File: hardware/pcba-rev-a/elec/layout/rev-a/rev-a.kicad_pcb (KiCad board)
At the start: 4 copper layers, 160 x 100 mm, 154 parts

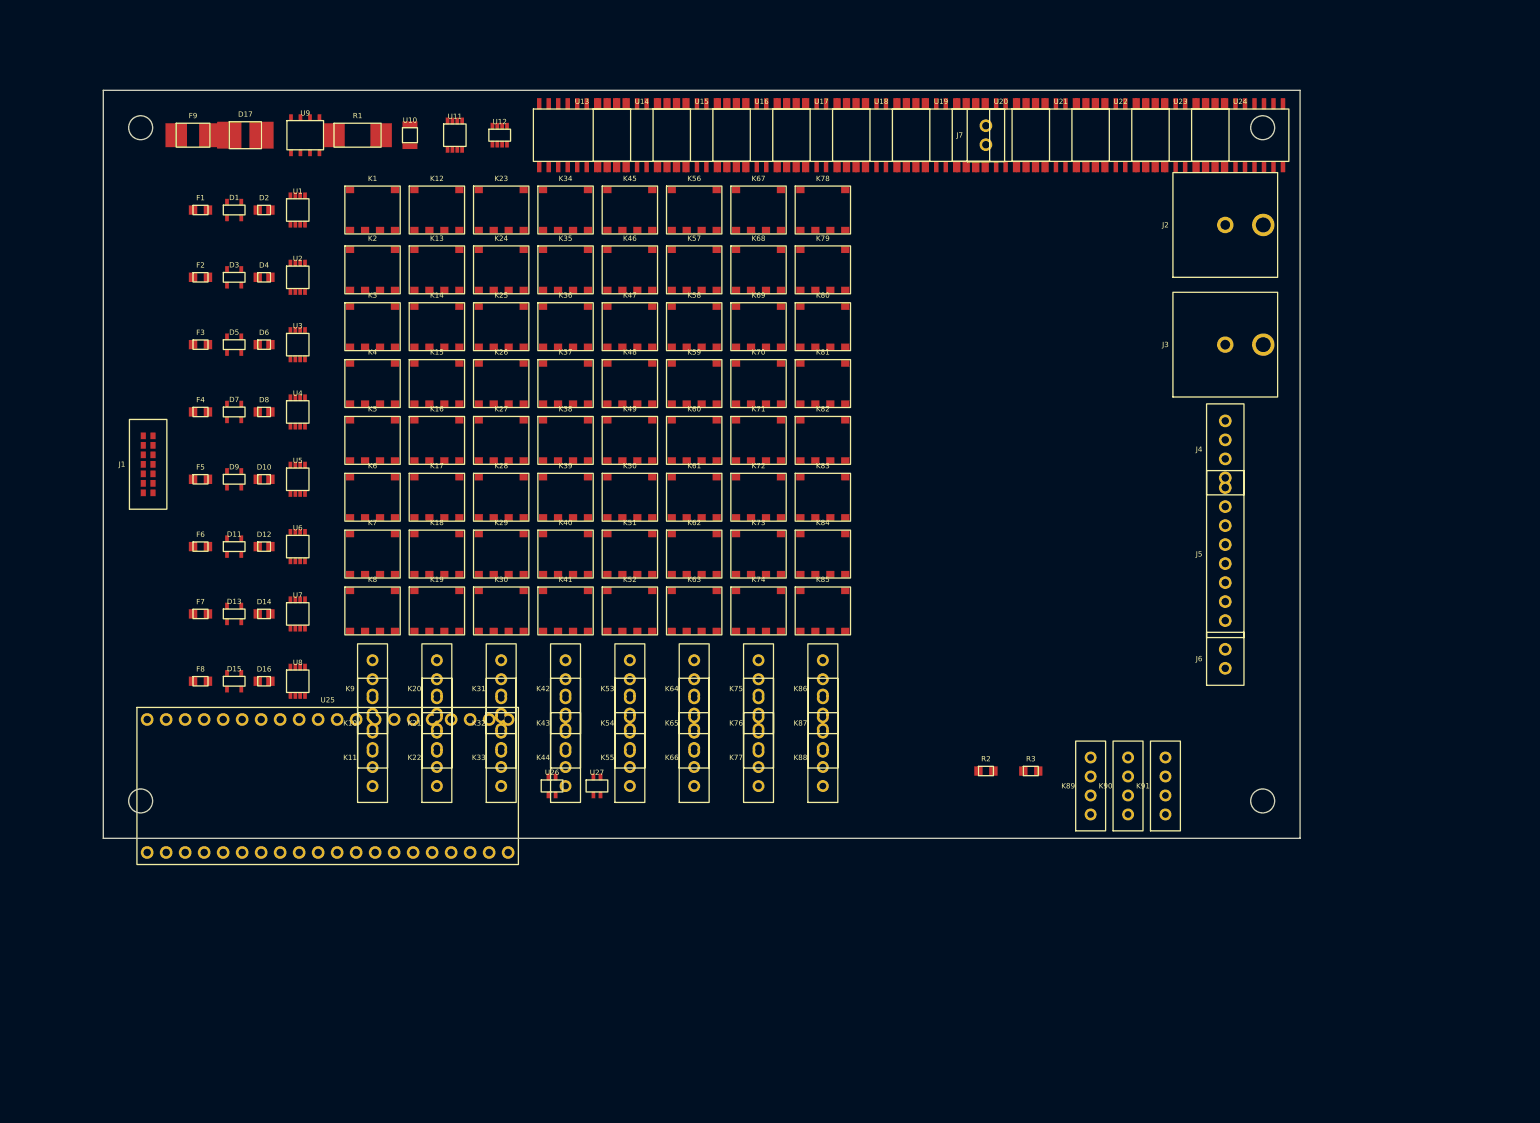
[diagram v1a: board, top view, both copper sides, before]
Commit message: Rev A board: real KiCad library footprints, 3D bodies, DRC-clean floorplan
- gen_board.py now instantiates KiCad's installed library footprints
  (Omron G6K-2F-Y, StandexMeder SIL reed, SOIC-20W, Pico 2 module,
  Amphenol BNC, headers, passives) with nets injected into their pads -
  3D viewer shows actual component bodies.
- Board grown 160x100 -> 200x146: measured courtyards total ~12,100 mm2
  (76% utilization on the old outline - unplaceable). Iterated against
  kicad-cli DRC to zero courtyard overlaps and zero edge violations
  (was 126 + 7 on first pass; bugs: Pico rotated long-axis horizontal,
  sink pitch vs BNCs, relay field touching reed bank, header rotations).
- project_spec.json outline updated with rationale.

Co-Authored-By: Claude Fable 5 <noreply@anthropic.com>
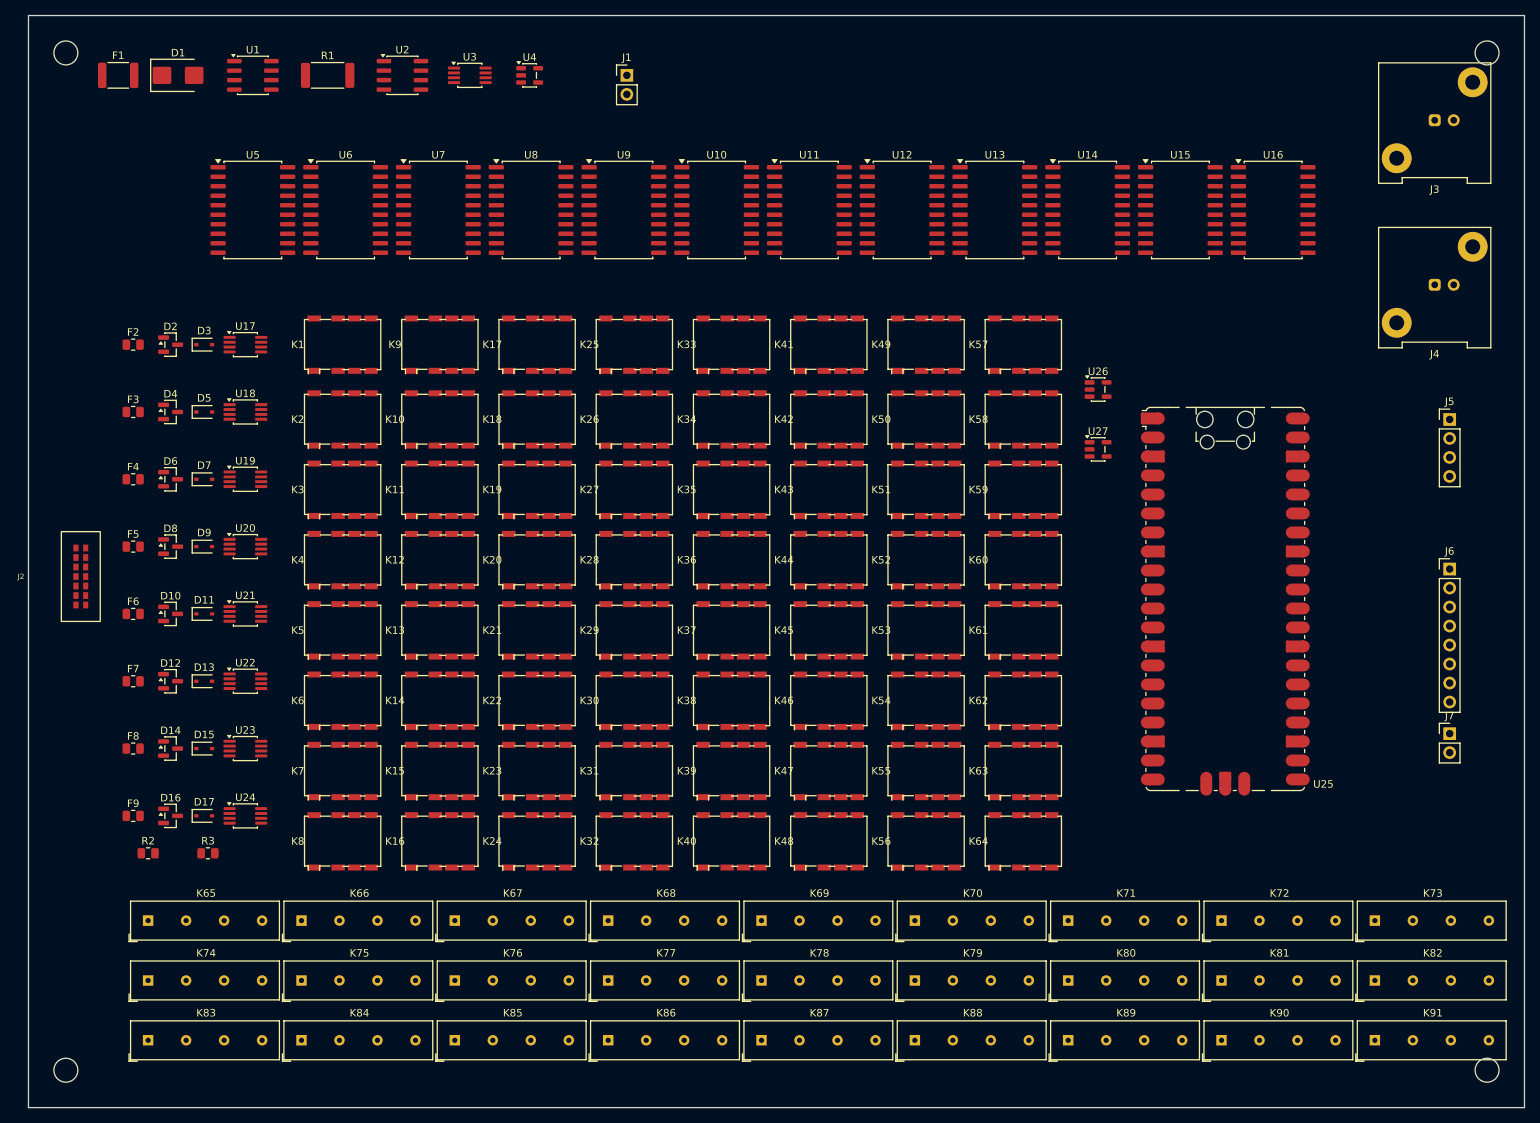
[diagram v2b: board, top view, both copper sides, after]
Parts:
- D1: value (none) -> D_SMB; footprint EE:SOT23 -> Diode_SMD:D_SMB
- D10, D12, D14, D16, D2, D4, D6, D8: value (none) -> SOT-23; footprint EE:SOD323 -> Package_TO_SOT_SMD:SOT-23
- D11, D13, D15, D3, D5, D7, D9: value (none) -> D_SOD-323; footprint EE:SOT23 -> Diode_SMD:D_SOD-323
- D17: value (none) -> D_SOD-323; footprint EE:SMB -> Diode_SMD:D_SOD-323
- F1: value (none) -> Fuse_1812_4532Metric; footprint EE:PTC0805 -> Fuse:Fuse_1812_4532Metric
- F2, F3, F4, F5, F6, F7, F8: value (none) -> R_0805_2012Metric; footprint EE:PTC0805 -> Resistor_SMD:R_0805_2012Metric
- F9: value (none) -> R_0805_2012Metric; footprint EE:FUSE1812 -> Resistor_SMD:R_0805_2012Metric
- J1: value (none) -> PinHeader_1x02_P2.54mm_Vertical; footprint EE:SEAF14 -> Connector_PinHeader_2.54mm:PinHeader_1x02_P2.54mm_Vertical
- J2: footprint EE:BNC_TH -> EE:SEAF14
- J3: value (none) -> BNC_Amphenol_031-5539_Vertical; footprint EE:BNC_TH -> Connector_Coaxial:BNC_Amphenol_031-5539_Vertical
- J4: value (none) -> BNC_Amphenol_031-5539_Vertical; footprint EE:HDR4 -> Connector_Coaxial:BNC_Amphenol_031-5539_Vertical
- J5: value (none) -> PinHeader_1x04_P2.54mm_Vertical; footprint EE:HDR8 -> Connector_PinHeader_2.54mm:PinHeader_1x04_P2.54mm_Vertical
- J6: value (none) -> PinHeader_1x08_P2.54mm_Vertical; footprint EE:HDR2 -> Connector_PinHeader_2.54mm:PinHeader_1x08_P2.54mm_Vertical
- J7: value (none) -> PinHeader_1x02_P2.54mm_Vertical; footprint EE:HDR2 -> Connector_PinHeader_2.54mm:PinHeader_1x02_P2.54mm_Vertical
- K1, K12, K13, K14, K15, K16, K17, K18, K19, K2, K23, K24, K25, K26, K27, K28, K29, K3, K30, K34, K35, K36, K37, K38, K39, K4, K40, K41, K45, K46, K47, K48, K49, K5, K50, K51, K52, K56, K57, K58, K59, K6, K60, K61, K62, K63, K7, K8: value (none) -> Relay_DPDT_Omron_G6K-2F-Y; footprint EE:RELAY_G6K2FY -> Relay_SMD:Relay_DPDT_Omron_G6K-2F-Y
- K10, K11, K20, K21, K22, K31, K32, K33, K42, K43, K44, K53, K54, K55, K64, K9: value (none) -> Relay_DPDT_Omron_G6K-2F-Y; footprint EE:REED_SIP4 -> Relay_SMD:Relay_DPDT_Omron_G6K-2F-Y
- K65, K66, K75, K76, K77, K86, K87, K88, K89, K90, K91: value (none) -> Relay_SPST_StandexMeder_SIL_Form1A; footprint EE:REED_SIP4 -> Relay_THT:Relay_SPST_StandexMeder_SIL_Form1A
- K67, K68, K69, K70, K71, K72, K73, K74, K78, K79, K80, K81, K82, K83, K84, K85: value (none) -> Relay_SPST_StandexMeder_SIL_Form1A; footprint EE:RELAY_G6K2FY -> Relay_THT:Relay_SPST_StandexMeder_SIL_Form1A
- R1: value (none) -> R_2512_6332Metric; footprint EE:R2512 -> Resistor_SMD:R_2512_6332Metric
- R2, R3: value (none) -> R_0805_2012Metric; footprint EE:R0805 -> Resistor_SMD:R_0805_2012Metric
- U1, U2: value (none) -> SOIC-8_3.9x4.9mm_P1.27mm; footprint EE:MSOP8 -> Package_SO:SOIC-8_3.9x4.9mm_P1.27mm
- U10: value (none) -> SOIC-20W_7.5x12.8mm_P1.27mm; footprint EE:SON8 -> Package_SO:SOIC-20W_7.5x12.8mm_P1.27mm
- U11, U5, U6, U7, U8: value (none) -> SOIC-20W_7.5x12.8mm_P1.27mm; footprint EE:MSOP8 -> Package_SO:SOIC-20W_7.5x12.8mm_P1.27mm
- U12: value (none) -> SOIC-20W_7.5x12.8mm_P1.27mm; footprint EE:SOT23_8 -> Package_SO:SOIC-20W_7.5x12.8mm_P1.27mm
- U13, U14, U15, U16: value (none) -> SOIC-20W_7.5x12.8mm_P1.27mm; footprint EE:SOIC20W -> Package_SO:SOIC-20W_7.5x12.8mm_P1.27mm
- U17, U18, U19, U20, U21, U22, U23, U24: value (none) -> MSOP-8_3x3mm_P0.65mm; footprint EE:SOIC20W -> Package_SO:MSOP-8_3x3mm_P0.65mm
- U25: value (none) -> RaspberryPi_Pico_SMD_HandSolder; footprint EE:PICO2_MODULE -> Module:RaspberryPi_Pico_SMD_HandSolder
- U26: value (none) -> SOT-23-5; footprint EE:SOT23_5W -> Package_TO_SOT_SMD:SOT-23-5
- U27: value (none) -> SOT-23-5; footprint EE:SOT23_5E -> Package_TO_SOT_SMD:SOT-23-5
- U3: value (none) -> MSOP-8_3x3mm_P0.65mm; footprint EE:MSOP8 -> Package_SO:MSOP-8_3x3mm_P0.65mm
- U4: value (none) -> SOT-23-5; footprint EE:MSOP8 -> Package_TO_SOT_SMD:SOT-23-5
- U9: value (none) -> SOIC-20W_7.5x12.8mm_P1.27mm; footprint EE:SOIC8_BUCK -> Package_SO:SOIC-20W_7.5x12.8mm_P1.27mm
- moved U24 161.2 mm to (69.0, 147.0)
- moved J2 160.1 mm to (47.0, 115.0)
- moved U23 149.5 mm to (69.0, 138.0)
- moved U22 137.9 mm to (69.0, 129.0)
- moved U21 126.4 mm to (69.0, 120.0)
- moved U25 122.6 mm to (200.0, 118.0)
- moved K83 115.8 mm to (56.0, 177.0)
- moved U20 115.0 mm to (69.0, 111.0)
- moved R2 112.5 mm to (56.0, 152.0)
- moved R3 110.5 mm to (64.0, 152.0)
- moved U19 103.8 mm to (69.0, 102.0)
- moved K78 103.3 mm to (138.0, 169.0)
- moved K67 103.3 mm to (97.0, 161.0)
- moved K82 103.2 mm to (220.0, 169.0)
- moved J7 101.2 mm to (230.0, 136.0), turned to 0 degrees
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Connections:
- D1 pad 1: NODE_P1 -> +24V
- D1 pad 2: (no net) -> GND
- D10 pad 2: GND -> (no net)
- D11 pad 1: NODE_KFN -> NODE_KFP
- D11 pad 2: (no net) -> GND
- D12 pad 2: GND -> (no net)
- D13 pad 1: NODE_KSP -> NODE_KFN
- D13 pad 2: (no net) -> GND
- D14 pad 2: GND -> (no net)
- D15 pad 1: NODE_KSN -> NODE_KSP
- D15 pad 2: (no net) -> GND
- D16 pad 2: GND -> (no net)
- D17 pad 1: +24V -> NODE_KSN
- D2 pad 2: GND -> (no net)
- D3 pad 1: NODE_P2 -> NODE_P1
- D3 pad 2: (no net) -> GND
- D4 pad 2: GND -> (no net)
- D5 pad 1: NODE_P3 -> NODE_P2
- D5 pad 2: (no net) -> GND
- D6 pad 2: GND -> (no net)
- D7 pad 1: NODE_P4 -> NODE_P3
- D7 pad 2: (no net) -> GND
- D8 pad 2: GND -> (no net)
- D9 pad 1: NODE_KFP -> NODE_P4
- D9 pad 2: (no net) -> GND
- F1 pad 1: TIP_P1 -> +24V
- F1 pad 2: NODE_P1 -> +24V
- F2 pad 1: TIP_P2 -> TIP_P1
- F2 pad 2: NODE_P2 -> NODE_P1
- F3 pad 1: TIP_P3 -> TIP_P2
- F3 pad 2: NODE_P3 -> NODE_P2
- F4 pad 1: TIP_P4 -> TIP_P3
- F4 pad 2: NODE_P4 -> NODE_P3
- F5 pad 1: TIP_KFP -> TIP_P4
- F5 pad 2: NODE_KFP -> NODE_P4
- F6 pad 1: TIP_KFN -> TIP_KFP
- F6 pad 2: NODE_KFN -> NODE_KFP
- F7 pad 1: TIP_KSP -> TIP_KFN
- F7 pad 2: NODE_KSP -> NODE_KFN
- F8 pad 1: TIP_KSN -> TIP_KSP
- F8 pad 2: NODE_KSN -> NODE_KSP
- F9 pad 1: +24V -> TIP_KSN
- F9 pad 2: +24V -> NODE_KSN
- J1 pad 1: TIP_P1 -> +24V
- J1 pad 2: TIP_P2 -> GND
- J2 pad 1: SCOPE_A -> TIP_P1
- J2 pad 2: GND -> TIP_P2
- J3 pad 1: SCOPE_B -> SCOPE_A
- J4 pad 1: DMM_HI -> SCOPE_B
- J4 pad 2: DMM_LO -> GND
- J5 pad 1: DAQ_1 -> DMM_HI
- J5 pad 2: DAQ_2 -> DMM_LO
- J5 pad 3: LOGIC_1 -> GND_REF
- J5 pad 4: LOGIC_2 -> GND
- J6 pad 1: PWR_INJ -> DAQ_1
- J6 pad 2: GND -> DAQ_2
- J7 pad 1: +24V -> PWR_INJ
- K1 pad 3: PBANK_P1 -> GBANK_P1
- K1 pad 5: GBANK_P1 -> PBANK_P1
- K10 pad 2: PBANK_P1 -> (no net)
- K10 pad 3: DMM_LO -> SCOPE_A
- K10 pad 4: (no net) -> GBANK_P2
- K11 pad 2: PBANK_P1 -> (no net)
- K11 pad 3: GND_REF -> SCOPE_B
- K11 pad 4: (no net) -> GBANK_P2
- K12 pad 3: PBANK_P2 -> DAQ_1
- K12 pad 4: NODE_P2 -> GBANK_P2
- K12 pad 5: GBANK_P2 -> (no net)
- K13 pad 3: SCOPE_A -> DAQ_2
- K14 pad 3: SCOPE_B -> LOGIC_1
- K15 pad 3: DAQ_1 -> LOGIC_2
- K16 pad 3: DAQ_2 -> PWR_INJ
- K17 pad 3: LOGIC_1 -> GBANK_P3
- K17 pad 4: GBANK_P2 -> NODE_P3
- K17 pad 5: (no net) -> PBANK_P3
- K18 pad 3: LOGIC_2 -> SCOPE_A
- K18 pad 4: GBANK_P2 -> GBANK_P3
- K19 pad 3: PWR_INJ -> SCOPE_B
- K19 pad 4: GBANK_P2 -> GBANK_P3
- K20 pad 2: PBANK_P2 -> (no net)
- K20 pad 3: DMM_HI -> DAQ_1
- K20 pad 4: (no net) -> GBANK_P3
- K21 pad 2: PBANK_P2 -> (no net)
- K21 pad 3: DMM_LO -> DAQ_2
- K21 pad 4: (no net) -> GBANK_P3
- K22 pad 2: PBANK_P2 -> (no net)
- K22 pad 3: GND_REF -> LOGIC_1
- K22 pad 4: (no net) -> GBANK_P3
- K23 pad 3: PBANK_P3 -> LOGIC_2
- K23 pad 4: NODE_P3 -> GBANK_P3
- K23 pad 5: GBANK_P3 -> (no net)
- K24 pad 3: SCOPE_A -> PWR_INJ
- K25 pad 3: SCOPE_B -> GBANK_P4
- K25 pad 4: GBANK_P3 -> NODE_P4
- K25 pad 5: (no net) -> PBANK_P4
- K26 pad 3: DAQ_1 -> SCOPE_A
- K26 pad 4: GBANK_P3 -> GBANK_P4
- K27 pad 3: DAQ_2 -> SCOPE_B
- K27 pad 4: GBANK_P3 -> GBANK_P4
- K28 pad 3: LOGIC_1 -> DAQ_1
- K28 pad 4: GBANK_P3 -> GBANK_P4
- K29 pad 3: LOGIC_2 -> DAQ_2
- K29 pad 4: GBANK_P3 -> GBANK_P4
- K30 pad 3: PWR_INJ -> LOGIC_1
- K30 pad 4: GBANK_P3 -> GBANK_P4
- K31 pad 2: PBANK_P3 -> (no net)
- K31 pad 3: DMM_HI -> LOGIC_2
- K31 pad 4: (no net) -> GBANK_P4
- K32 pad 2: PBANK_P3 -> (no net)
- K32 pad 3: DMM_LO -> PWR_INJ
- K32 pad 4: (no net) -> GBANK_P4
- K33 pad 2: PBANK_P3 -> (no net)
- K33 pad 3: GND_REF -> GBANK_KFP
- K33 pad 4: (no net) -> NODE_KFP
- K34 pad 3: PBANK_P4 -> SCOPE_A
- K34 pad 4: NODE_P4 -> GBANK_KFP
- K34 pad 5: GBANK_P4 -> (no net)
- K35 pad 3: SCOPE_A -> SCOPE_B
- K35 pad 4: GBANK_P4 -> GBANK_KFP
- K36 pad 3: SCOPE_B -> DAQ_1
- K36 pad 4: GBANK_P4 -> GBANK_KFP
- K37 pad 3: DAQ_1 -> DAQ_2
- K37 pad 4: GBANK_P4 -> GBANK_KFP
- K38 pad 3: DAQ_2 -> LOGIC_1
- K38 pad 4: GBANK_P4 -> GBANK_KFP
- K39 pad 3: LOGIC_1 -> LOGIC_2
- K39 pad 4: GBANK_P4 -> GBANK_KFP
- K40 pad 3: LOGIC_2 -> PWR_INJ
- K40 pad 4: GBANK_P4 -> GBANK_KFP
- K41 pad 3: PWR_INJ -> GBANK_KFN
- K41 pad 4: GBANK_P4 -> NODE_KFN
- K41 pad 5: (no net) -> PBANK_KFN
- K42 pad 2: PBANK_P4 -> (no net)
- K42 pad 3: DMM_HI -> SCOPE_A
- K42 pad 4: (no net) -> GBANK_KFN
- K43 pad 2: PBANK_P4 -> (no net)
- K43 pad 3: DMM_LO -> SCOPE_B
- K43 pad 4: (no net) -> GBANK_KFN
- K44 pad 2: PBANK_P4 -> (no net)
- K44 pad 3: GND_REF -> DAQ_1
- K44 pad 4: (no net) -> GBANK_KFN
- K45 pad 3: PBANK_KFP -> DAQ_2
- K45 pad 4: NODE_KFP -> GBANK_KFN
- K45 pad 5: GBANK_KFP -> (no net)
- K46 pad 3: SCOPE_A -> LOGIC_1
- K46 pad 4: GBANK_KFP -> GBANK_KFN
- K47 pad 3: SCOPE_B -> LOGIC_2
- K47 pad 4: GBANK_KFP -> GBANK_KFN
- K48 pad 3: DAQ_1 -> PWR_INJ
- K48 pad 4: GBANK_KFP -> GBANK_KFN
- K49 pad 3: DAQ_2 -> GBANK_KSP
- K49 pad 4: GBANK_KFP -> NODE_KSP
- K49 pad 5: (no net) -> PBANK_KSP
- K50 pad 3: LOGIC_1 -> SCOPE_A
- K50 pad 4: GBANK_KFP -> GBANK_KSP
- K51 pad 3: LOGIC_2 -> SCOPE_B
- K51 pad 4: GBANK_KFP -> GBANK_KSP
- K52 pad 3: PWR_INJ -> DAQ_1
- K52 pad 4: GBANK_KFP -> GBANK_KSP
- K53 pad 2: PBANK_KFP -> (no net)
- K53 pad 3: DMM_HI -> DAQ_2
- K53 pad 4: (no net) -> GBANK_KSP
- K54 pad 2: PBANK_KFP -> (no net)
- K54 pad 3: DMM_LO -> LOGIC_1
- K54 pad 4: (no net) -> GBANK_KSP
- K55 pad 2: PBANK_KFP -> (no net)
- K55 pad 3: GND_REF -> LOGIC_2
- K55 pad 4: (no net) -> GBANK_KSP
- K56 pad 3: PBANK_KFN -> PWR_INJ
- K56 pad 4: NODE_KFN -> GBANK_KSP
- K56 pad 5: GBANK_KFN -> (no net)
- K57 pad 3: SCOPE_A -> GBANK_KSN
- K57 pad 4: GBANK_KFN -> NODE_KSN
- K57 pad 5: (no net) -> PBANK_KSN
- K58 pad 3: SCOPE_B -> SCOPE_A
- K58 pad 4: GBANK_KFN -> GBANK_KSN
- K59 pad 3: DAQ_1 -> SCOPE_B
- K59 pad 4: GBANK_KFN -> GBANK_KSN
- K60 pad 3: DAQ_2 -> DAQ_1
- K60 pad 4: GBANK_KFN -> GBANK_KSN
- K61 pad 3: LOGIC_1 -> DAQ_2
- K61 pad 4: GBANK_KFN -> GBANK_KSN
- K62 pad 3: LOGIC_2 -> LOGIC_1
- K62 pad 4: GBANK_KFN -> GBANK_KSN
- K63 pad 3: PWR_INJ -> LOGIC_2
- K63 pad 4: GBANK_KFN -> GBANK_KSN
- K64 pad 2: PBANK_KFN -> (no net)
- K64 pad 3: DMM_HI -> PWR_INJ
- K64 pad 4: (no net) -> GBANK_KSN
- K65 pad 3: DMM_LO -> DMM_HI
- K66 pad 3: GND_REF -> DMM_LO
- K67 pad 3: PBANK_KSP -> GND_REF
- K67 pad 5: GBANK_KSP -> (no net)
- K68 pad 3: SCOPE_A -> DMM_HI
- K69 pad 3: SCOPE_B -> DMM_LO
- K70 pad 3: DAQ_1 -> GND_REF
- K71 pad 3: DAQ_2 -> DMM_HI
- K72 pad 3: LOGIC_1 -> DMM_LO
- K73 pad 3: LOGIC_2 -> GND_REF
- K74 pad 3: PWR_INJ -> DMM_HI
- K75 pad 3: DMM_HI -> DMM_LO
- K76 pad 3: DMM_LO -> GND_REF
- K77 pad 3: GND_REF -> DMM_HI
- K78 pad 3: PBANK_KSN -> DMM_LO
- K78 pad 5: GBANK_KSN -> (no net)
- K79 pad 3: SCOPE_A -> GND_REF
- K80 pad 3: SCOPE_B -> DMM_HI
- K81 pad 3: DAQ_1 -> DMM_LO
- K82 pad 3: DAQ_2 -> GND_REF
- K83 pad 3: LOGIC_1 -> DMM_HI
- K84 pad 3: LOGIC_2 -> DMM_LO
- K85 pad 3: PWR_INJ -> GND_REF
- K9 pad 2: PBANK_P1 -> (no net)
- K9 pad 3: DMM_HI -> GBANK_P2
- K9 pad 4: (no net) -> NODE_P2
- U1 pad 7: (no net) -> +24V
- U1 pad 8: +3V3_ANA -> +5V_COIL
- U10 pad 1: +5V_COIL -> (no net)
- U10 pad 2: GND -> +5V_COIL
- U10 pad 3: (no net) -> SR_DATA
- U10 pad 8: +3V3_DIG -> (no net)
- U11 pad 1: +5V_COIL -> (no net)
- U11 pad 2: GND -> +5V_COIL
- U11 pad 3: (no net) -> SR_DATA
- U11 pad 8: +3V3_ANA -> (no net)
- U12 pad 1: SDA -> (no net)
- U12 pad 2: SCL -> +5V_COIL
- U12 pad 3: (no net) -> SR_DATA
- U12 pad 5: GND -> (no net)
- U12 pad 6: +3V3_DIG -> (no net)
- U17 pad 1: (no net) -> NODE_P1
- U17 pad 2: +5V_COIL -> (no net)
- U17 pad 3: SR_DATA -> (no net)
- U17 pad 4: (no net) -> GND
- U17 pad 8: (no net) -> +3V3_ANA
- U18 pad 1: (no net) -> NODE_P2
- U18 pad 2: +5V_COIL -> (no net)
- U18 pad 3: SR_DATA -> (no net)
- U18 pad 4: (no net) -> GND
- U18 pad 8: (no net) -> +3V3_ANA
- U19 pad 1: (no net) -> NODE_P3
- U19 pad 2: +5V_COIL -> (no net)
- U19 pad 3: SR_DATA -> (no net)
- U19 pad 4: (no net) -> GND
- U19 pad 8: (no net) -> +3V3_ANA
- U2 pad 1: (no net) -> +5V_COIL
- U2 pad 8: +3V3_ANA -> +3V3_DIG
- U20 pad 1: (no net) -> NODE_P4
- U20 pad 2: +5V_COIL -> (no net)
- U20 pad 3: SR_DATA -> (no net)
- U20 pad 4: (no net) -> GND
- U20 pad 8: (no net) -> +3V3_ANA
- U21 pad 1: (no net) -> NODE_KFP
- U21 pad 2: +5V_COIL -> (no net)
- U21 pad 3: SR_DATA -> (no net)
- U21 pad 4: (no net) -> GND
- U21 pad 8: (no net) -> +3V3_ANA
- U22 pad 1: (no net) -> NODE_KFN
- U22 pad 2: +5V_COIL -> (no net)
- U22 pad 3: SR_DATA -> (no net)
- U22 pad 4: (no net) -> GND
- U22 pad 8: (no net) -> +3V3_ANA
- U23 pad 1: (no net) -> NODE_KSP
- U23 pad 2: +5V_COIL -> (no net)
- U23 pad 3: SR_DATA -> (no net)
- U23 pad 4: (no net) -> GND
- U23 pad 8: (no net) -> +3V3_ANA
- U24 pad 1: (no net) -> NODE_KSN
- U24 pad 2: +5V_COIL -> (no net)
- U24 pad 3: SR_DATA -> (no net)
- U24 pad 4: (no net) -> GND
- U24 pad 8: (no net) -> +3V3_ANA
- U3 pad 1: (no net) -> +5V_COIL
- U4 pad 1: (no net) -> SDA
- U4 pad 2: (no net) -> GND
- U4 pad 3: (no net) -> SCL
- U4 pad 4: GND -> (no net)
- U4 pad 5: (no net) -> +3V3_DIG
- U5 pad 2: (no net) -> +5V_COIL
- U5 pad 3: (no net) -> SR_DATA
- U5 pad 4: GND -> (no net)
- U5 pad 8: +3V3_ANA -> (no net)
- U6 pad 2: (no net) -> +5V_COIL
- U6 pad 3: (no net) -> SR_DATA
- U6 pad 4: GND -> (no net)
- U6 pad 8: +3V3_ANA -> (no net)
- U7 pad 2: (no net) -> +5V_COIL
- U7 pad 3: (no net) -> SR_DATA
- U7 pad 4: GND -> (no net)
- U7 pad 8: +3V3_ANA -> (no net)
- U8 pad 2: (no net) -> +5V_COIL
- U8 pad 3: (no net) -> SR_DATA
- U8 pad 4: GND -> (no net)
- U8 pad 8: +3V3_ANA -> (no net)
- U9 pad 2: (no net) -> +5V_COIL
- U9 pad 3: (no net) -> SR_DATA
- U9 pad 7: +24V -> (no net)
- U9 pad 8: +5V_COIL -> (no net)
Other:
- board size 160 x 100 mm -> 200 x 146 mm
- board text added: "ANALOG ISLAND - reed bank + references"
- board text removed: "ANALOG ISLAND - moat, guard DMM_HI/LO"

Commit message: Rev A DFM pass: gate script + fixes — DRC and DFM both clean
- scripts/dfm_check.py: assembly-rule gate KiCad DRC doesn't cover
  (3 mm edge clearance, 3.5 mm mounting-hole keepout, 0.4 mm courtyard
  gap for rework, fiducial count); writes output/dfm_profile_check.json
  like the Tile-0 pipeline; exits nonzero on FAIL.
- Findings fixed: relay grid 0.10 mm vertical gaps -> 9.75 pitch; reed
  bank rode the east edge + corner mounting hole (SIL footprint origin
  is pin-1, body extends 18.3 mm) -> 8x3 bank shifted inboard, the 3
  reference reeds moved to a vertical column between the relay field
  and the Pico; SCOPE BNCs pulled off the top-right hole; supervisors
  relocated clear of the BNC; 3 assembly fiducials added.
- Final: DRC courtyard/edge clean, DFM gate PASS (157 components).

Co-Authored-By: Claude Fable 5 <noreply@anthropic.com>
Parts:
- added FID1: Fiducial_1mm_Mask2mm, Fiducial:Fiducial_1mm_Mask2mm, F.Cu at (78.0, 77.0)
- added FID2: Fiducial_1mm_Mask2mm, Fiducial:Fiducial_1mm_Mask2mm, F.Cu at (235.0, 154.0)
- added FID3: Fiducial_1mm_Mask2mm, Fiducial:Fiducial_1mm_Mask2mm, F.Cu at (48.0, 156.0)
- moved K73 154.2 mm to (66.0, 169.5)
- moved K81 133.8 mm to (66.0, 177.5)
- moved K82 133.4 mm to (86.9, 177.5)
- moved K89 81.2 mm to (184.0, 96.0), turned to 90 degrees
- moved K90 62.0 mm to (184.0, 117.0), turned to 90 degrees
- moved K88 53.8 mm to (212.3, 177.5)
- moved K87 53.4 mm to (191.4, 177.5)
- moved K91 53.1 mm to (184.0, 138.0), turned to 90 degrees
- moved K86 53.0 mm to (170.5, 177.5)
- moved K85 52.6 mm to (149.6, 177.5)
- moved K84 52.2 mm to (128.7, 177.5)
- moved K83 51.8 mm to (107.8, 177.5)
- moved K80 33.3 mm to (212.3, 169.5)
- moved K79 32.9 mm to (191.4, 169.5)
- moved K78 32.5 mm to (170.5, 169.5)
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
